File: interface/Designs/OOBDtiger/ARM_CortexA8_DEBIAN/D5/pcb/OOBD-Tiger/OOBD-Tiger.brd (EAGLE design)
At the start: 63.4 x 38.2 mm, 123 parts, among them IC1 ADM3053M, IC2 ADM3053M, IC4 DS3231, U1 SY6280, U10 MP1482DS, U2 SN65HVD230(SO8), U3 SY6280, U6 SN65HVD230(SO8)

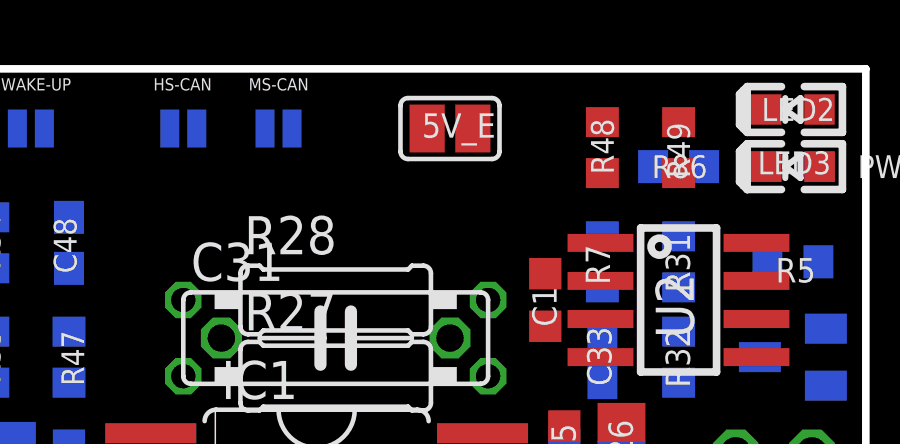
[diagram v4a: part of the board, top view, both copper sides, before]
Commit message: small modifications on schematics/board (signal re-alignment only)
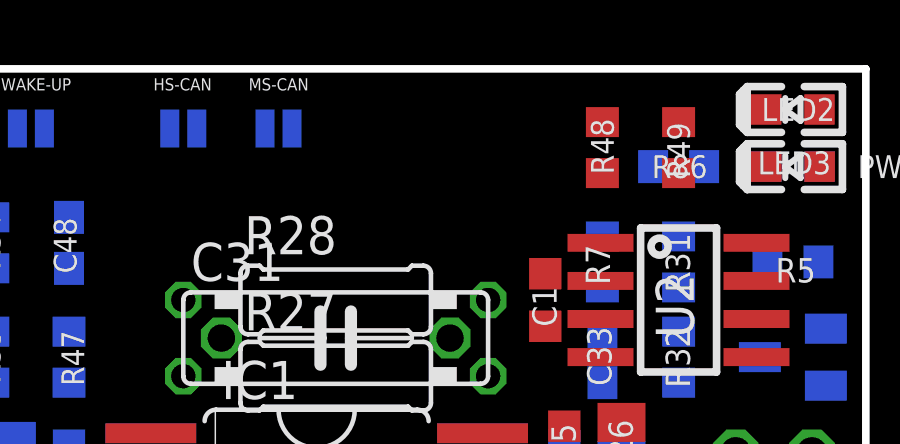
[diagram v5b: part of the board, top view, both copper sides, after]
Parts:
- removed 5V_E: Close, jumper:SJ
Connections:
- net P3_20/LED2 renamed LED2
- removed net N$12: 5V_E.1, C53.1, C54.1, C55.1, C56.1, L11.2, R70.2
- removed net P3_21/LED3: R48.1
- new net LED1: AM3352-SOM-EVB-PLATFORM.4-21, R48.1
- net +5V: now also C53.1, C54.1, C55.1, C56.1, L11.2, R70.2; no longer 5V_E.2
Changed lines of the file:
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@@
 <?xml version="1.0" encoding="utf-8"?>
 <!DOCTYPE eagle SYSTEM "eagle.dtd">
-<eagle version="7.6.0">
+<eagle version="6.4">
 <drawing>
 <settings>
@@
 <layer number="37" name="tTest" color="7" fill="1" visible="no" active="yes"/>
 <layer number="38" name="bTest" color="7" fill="1" visible="no" active="yes"/>
-<layer number="39" name="tKeepout" color="4" fill="11" visible="yes" active="yes"/>
-<layer number="40" name="bKeepout" color="3" fill="11" visible="yes" active="yes"/>
+<layer number="39" name="tKeepout" color="4" fill="11" visible="no" active="yes"/>
+<layer number="40" name="bKeepout" color="3" fill="11" visible="no" active="yes"/>
 <layer number="41" name="tRestrict" color="4" fill="10" visible="no" active="yes"/>
 <layer number="42" name="bRestrict" color="3" fill="10" visible="no" active="yes"/>
@@
 <layer number="46" name="Milling" color="3" fill="1" visible="no" active="yes"/>
 <layer number="47" name="Measures" color="7" fill="1" visible="no" active="yes"/>
-<layer number="48" name="Document" color="5" fill="1" visible="no" active="yes"/>
+<layer number="48" name="Document" color="5" fill="1" visible="yes" active="yes"/>
 <layer number="49" name="Reference" color="7" fill="1" visible="no" active="yes"/>
 <layer number="50" name="dxf" color="7" fill="1" visible="no" active="yes"/>
@@
 <layer number="230" name="230bmp" color="7" fill="1" visible="no" active="yes"/>
 <layer number="231" name="231bmp" color="7" fill="1" visible="no" active="yes"/>
-<layer number="232" name="Eagle3D_PG2" color="7" fill="1" visible="yes" active="yes"/>
-<layer number="233" name="Eagle3D_PG3" color="7" fill="1" visible="yes" active="yes"/>
+<layer number="232" name="Eagle3D_PG2" color="7" fill="1" visible="no" active="yes"/>
+<layer number="233" name="Eagle3D_PG3" color="7" fill="1" visible="no" active="yes"/>
 <layer number="248" name="Housing" color="7" fill="1" visible="no" active="yes"/>
 <layer number="249" name="Edge" color="7" fill="1" visible="no" active="yes"/>
@@
 <wire x1="0" y1="38.184" x2="63.391" y2="38.184" width="0.254" layer="20"/>
 <wire x1="63.391" y1="38.184" x2="63.391" y2="0" width="0.254" layer="20"/>
-<wire x1="55" y1="0" x2="55" y2="45" width="0.254" layer="48" style="shortdash"/>
-<wire x1="0" y1="45" x2="55" y2="45" width="0.254" layer="48" style="shortdash"/>
 <polygon width="0.4064" layer="41">
 <vertex x="41.5925" y="7.62"/>
@@
 <pass name="Default">
 <param name="RoutingGrid" value="50mil"/>
-<param name="AutoGrid" value="1"/>
-<param name="Efforts" value="2"/>
-<param name="TopRouterVariant" value="1"/>
 <param name="tpViaShape" value="round"/>
-<param name="PrefDir.1" value="a"/>
+<param name="PrefDir.1" value="|"/>
 <param name="PrefDir.2" value="0"/>
 <param name="PrefDir.3" value="0"/>
@@
 <param name="PrefDir.14" value="0"/>
 <param name="PrefDir.15" value="0"/>
-<param name="PrefDir.16" value="a"/>
+<param name="PrefDir.16" value="-"/>
 <param name="cfVia" value="8"/>
 <param name="cfNonPref" value="5"/>
@@
 <attribute name="NAME" x="28.956" y="18.669" size="0.762" layer="25" font="vector" ratio="11"/>
 <attribute name="VALUE" x="28.448" y="18.923" size="0.4064" layer="27" ratio="20"/>
-</element>
-<element name="5V_E" library="jumper" package="SJ" value="Close" x="49.53" y="36.195" smashed="yes" rot="R180">
-<attribute name="NAME" x="51.054" y="36.703" size="0.8128" layer="25" font="vector" ratio="11" rot="R180"/>
-<attribute name="VALUE" x="50.5269" y="36.703" size="0.4064" layer="27" rot="R180"/>
-<attribute name="VALUE" x="50.419" y="36.068" size="0.4064" layer="27" ratio="20" rot="R180"/>
 </element>
 <element name="C51" library="SparkFun-Capacitors" package="PANASONIC_D" value="470uF/25V/LOWESR/105C" x="11.43" y="19.05" smashed="yes" rot="R270">
@@
 <contactref element="C6" pad="1"/>
 <contactref element="U1" pad="5"/>
-<contactref element="5V_E" pad="2"/>
 <contactref element="R86" pad="1"/>
 <contactref element="AM3352-SOM-EVB-PLATFORM" pad="3-1"/>
@@
 <contactref element="IC2" pad="6"/>
 <contactref element="OOBDPICAN" pad="1"/>
-<wire x1="48.768" y1="36.195" x2="58" y2="34.925" width="0" layer="19" extent="1-16"/>
-<wire x1="39.5558" y1="20.955" x2="48.768" y2="36.195" width="0" layer="19" extent="1-16"/>
+<contactref element="L11" pad="2"/>
+<contactref element="C53" pad="1"/>
+<contactref element="R70" pad="2"/>
+<contactref element="C54" pad="1"/>
+<contactref element="C55" pad="1"/>
+<contactref element="C56" pad="1"/>
+<wire x1="39.5558" y1="20.955" x2="58" y2="34.925" width="0" layer="19" extent="16-16"/>
 <wire x1="39.5558" y1="19.685" x2="39.5558" y2="20.955" width="0" layer="19" extent="1-16"/>
 <wire x1="36.83" y1="20.56" x2="39.5558" y2="20.955" width="0" layer="19" extent="16-16"/>
@@
 <wire x1="34.925" y1="20.685" x2="36.83" y2="20.56" width="0" layer="19" extent="16-16"/>
 <wire x1="34.925" y1="19.955" x2="34.925" y2="20.685" width="0" layer="19" extent="1-16"/>
-<wire x1="28.095" y1="14.195" x2="34.925" y2="19.955" width="0" layer="19" extent="1-16"/>
+<wire x1="30.695" y1="19.05" x2="34.925" y2="19.955" width="0" layer="19" extent="1-1"/>
+<wire x1="27.52" y1="19.05" x2="30.695" y2="19.05" width="0" layer="19" extent="1-1"/>
+<wire x1="24.345" y1="19.05" x2="27.52" y2="19.05" width="0" layer="19" extent="1-1"/>
+<wire x1="21.17" y1="19.05" x2="24.345" y2="19.05" width="0" layer="19" extent="1-1"/>
+<wire x1="21.17" y1="21.59" x2="21.17" y2="19.05" width="0" layer="19" extent="1-1"/>
+<wire x1="28.095" y1="14.195" x2="27.52" y2="19.05" width="0" layer="19" extent="1-16"/>
+<wire x1="23.57" y1="13.335" x2="28.095" y2="14.195" width="0" layer="19" extent="1-16"/>
 <wire x1="27.94" y1="6.477" x2="28.095" y2="14.195" width="0" layer="19" extent="1-16"/>
 <wire x1="30.48" y1="1.905" x2="27.94" y2="6.477" width="0" layer="19" extent="1-1"/>
-<wire x1="12.7301" y1="25.085" x2="28.095" y2="14.195" width="0" layer="19" extent="16-16"/>
+<wire x1="12.7301" y1="25.085" x2="21.17" y2="21.59" width="0" layer="19" extent="1-16"/>
 <wire x1="9.285" y1="33.655" x2="12.7301" y2="25.085" width="0" layer="19" extent="16-16"/>
 <wire x1="5.0499" y1="35.245" x2="9.285" y2="33.655" width="0" layer="19" extent="1-16"/>
@@
 <wire x1="11.43" y1="2.413" x2="14.315" y2="13.485" width="0" layer="19" extent="1-16"/>
 </signal>
-<signal name="P3_21/LED3">
-<contactref element="R48" pad="1"/>
-</signal>
-<signal name="P3_20/LED2">
+<signal name="LED2">
 <contactref element="R49" pad="1"/>
 <contactref element="AM3352-SOM-EVB-PLATFORM" pad="4-23"/>
@@
 <contactref element="PWR_LED" pad="A"/>
 <wire x1="56.3" y1="34.925" x2="60.071" y2="34.925" width="0" layer="19" extent="16-16"/>
-</signal>
-<signal name="N$12" class="1">
-<contactref element="L11" pad="2"/>
-<contactref element="C53" pad="1"/>
-<contactref element="R70" pad="2"/>
-<contactref element="C54" pad="1"/>
-<contactref element="5V_E" pad="1"/>
-<contactref element="C55" pad="1"/>
-<contactref element="C56" pad="1"/>
-<wire x1="30.695" y1="19.05" x2="50.292" y2="36.195" width="0" layer="19" extent="1-1"/>
-<wire x1="27.52" y1="19.05" x2="30.695" y2="19.05" width="0" layer="19" extent="1-1"/>
-<wire x1="24.345" y1="19.05" x2="27.52" y2="19.05" width="0" layer="19" extent="1-1"/>
-<wire x1="21.17" y1="19.05" x2="24.345" y2="19.05" width="0" layer="19" extent="1-1"/>
-<wire x1="21.17" y1="21.59" x2="21.17" y2="19.05" width="0" layer="19" extent="1-1"/>
-<wire x1="23.57" y1="13.335" x2="24.345" y2="19.05" width="0" layer="19" extent="1-1"/>
 </signal>
 <signal name="N$5">
@@
 <wire x1="57.15" y1="10.58" x2="44.265" y2="36.195" width="0" layer="19" extent="16-16"/>
 </signal>
+<signal name="LED1">
+<contactref element="AM3352-SOM-EVB-PLATFORM" pad="4-21"/>
+<contactref element="R48" pad="1"/>
+<wire x1="15.24" y1="6.477" x2="54.61" y2="34.71" width="0" layer="19" extent="1-1"/>
+</signal>
 </signals>
-<errors>
-</errors>
 </board>
 </drawing>

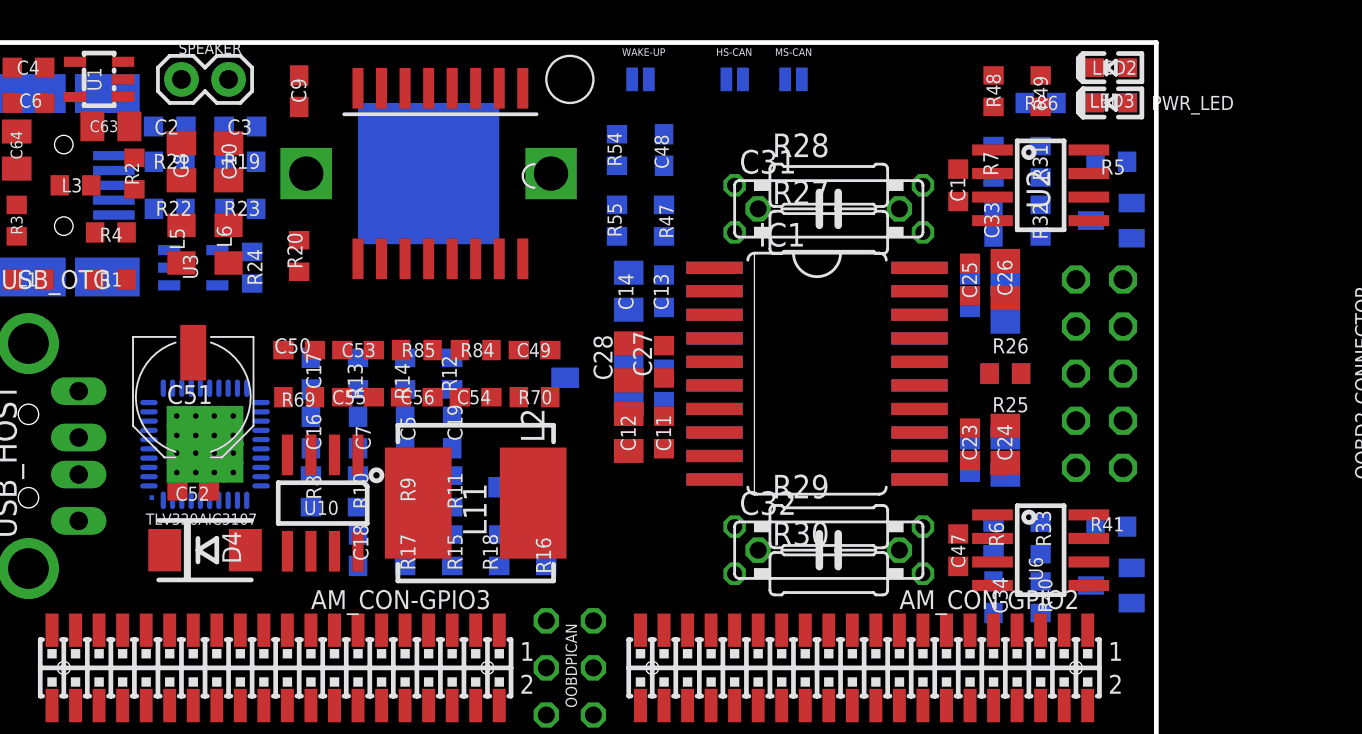
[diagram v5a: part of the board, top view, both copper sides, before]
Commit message: CAN-Transceiver SN65HVD230 shift to left from adm3053
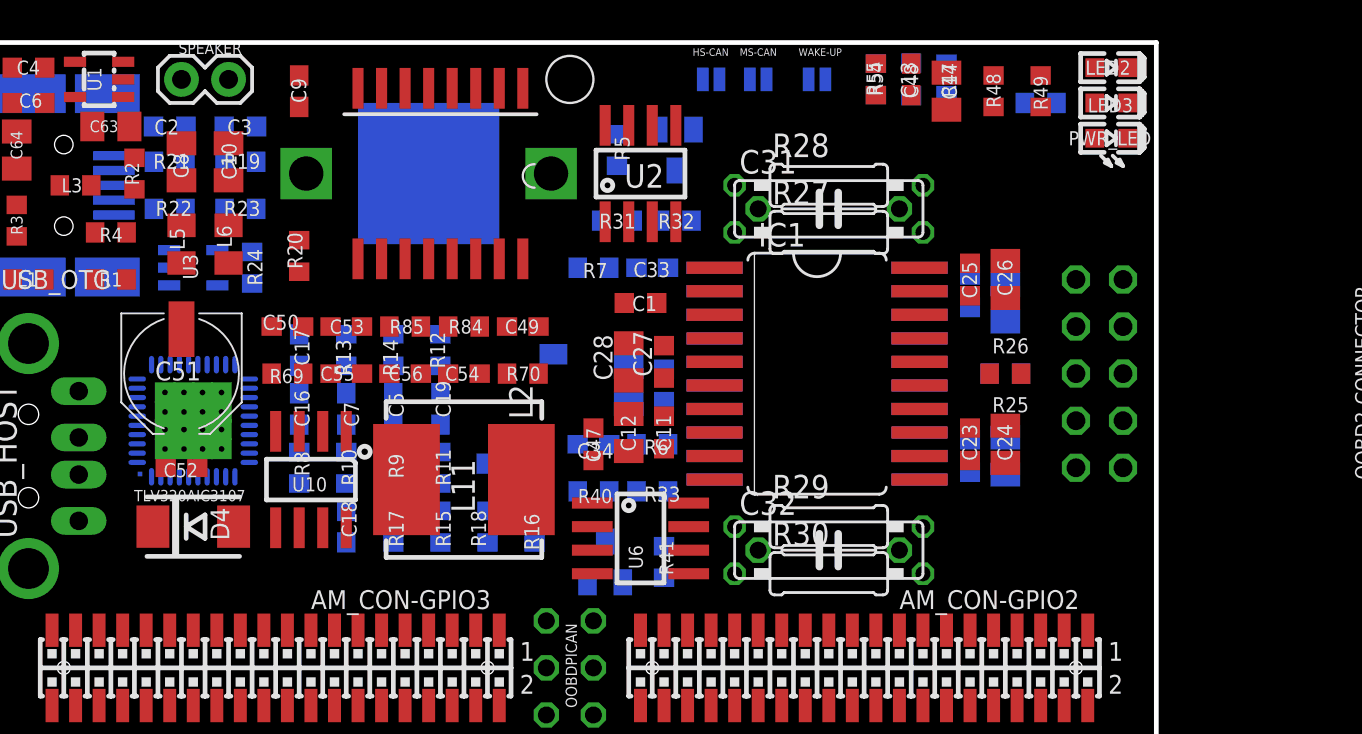
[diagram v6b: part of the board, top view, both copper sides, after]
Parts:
- moved D1 27.3 mm to (33.7, 10.2), turned to 0 degrees
- moved R5 26.7 mm to (34.3, 32.4), turned to 270 degrees
- moved R40 24.8 mm to (33.0, 14.0), turned to 0 degrees
- moved R41 24.2 mm to (36.8, 10.2), turned to 270 degrees
- moved D2 23.8 mm to (37.5, 32.4), turned to 180 degrees
- moved C34 23.1 mm to (33.0, 16.5), turned to 180 degrees
- moved R31 23.1 mm to (34.3, 28.6), turned to 180 degrees
- moved R7 22.3 mm to (33.0, 26.0), turned to 0 degrees
- moved U2 21.6 mm to (35.6, 31.1), turned to 0 degrees
- moved U6 21.6 mm to (35.6, 11.4)
- moved R33 21.1 mm to (36.2, 14.0), turned to 0 degrees
- moved C47 20.5 mm to (33.0, 16.5)
- moved C14 20.3 mm to (52.1, 35.6), flipped to the top
- moved R32 19.7 mm to (37.5, 28.6), turned to 180 degrees
- moved R6 19.1 mm to (36.2, 16.5), turned to 0 degrees
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
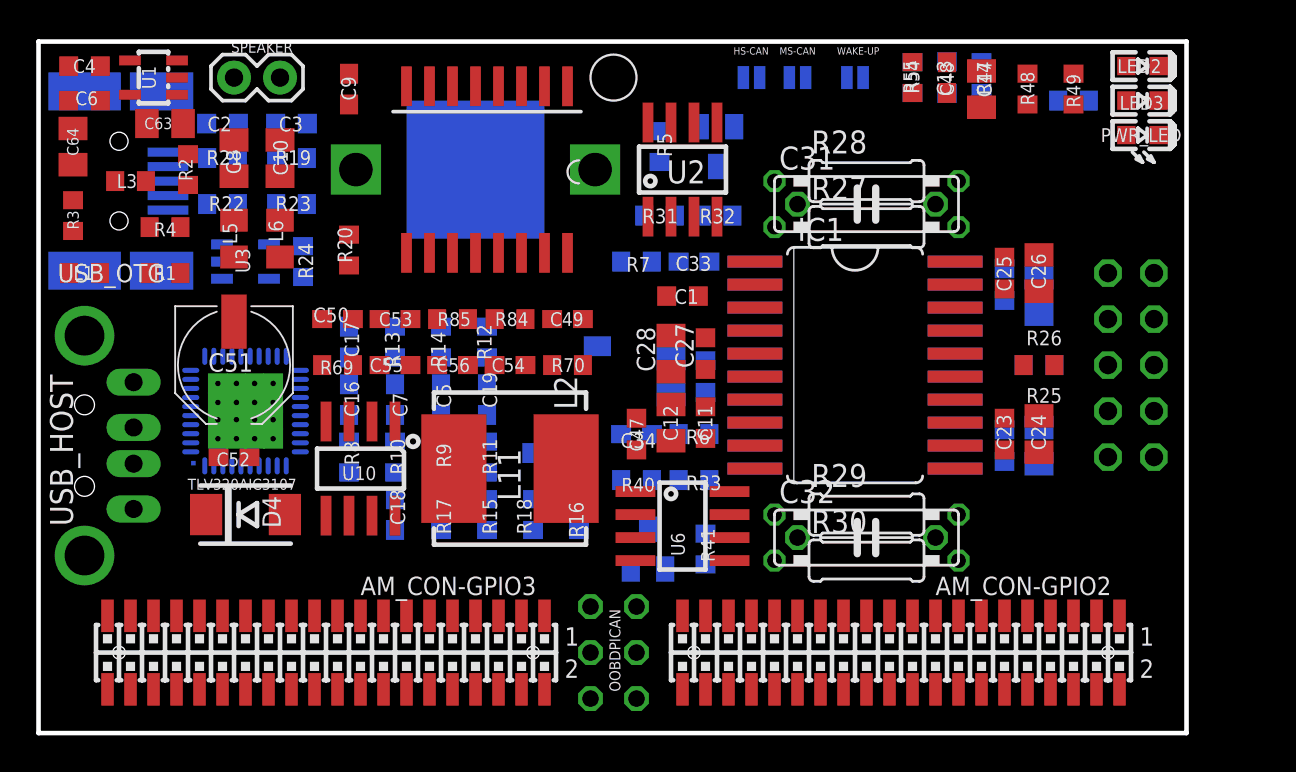
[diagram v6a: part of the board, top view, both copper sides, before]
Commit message: kleinerer Korrekturen
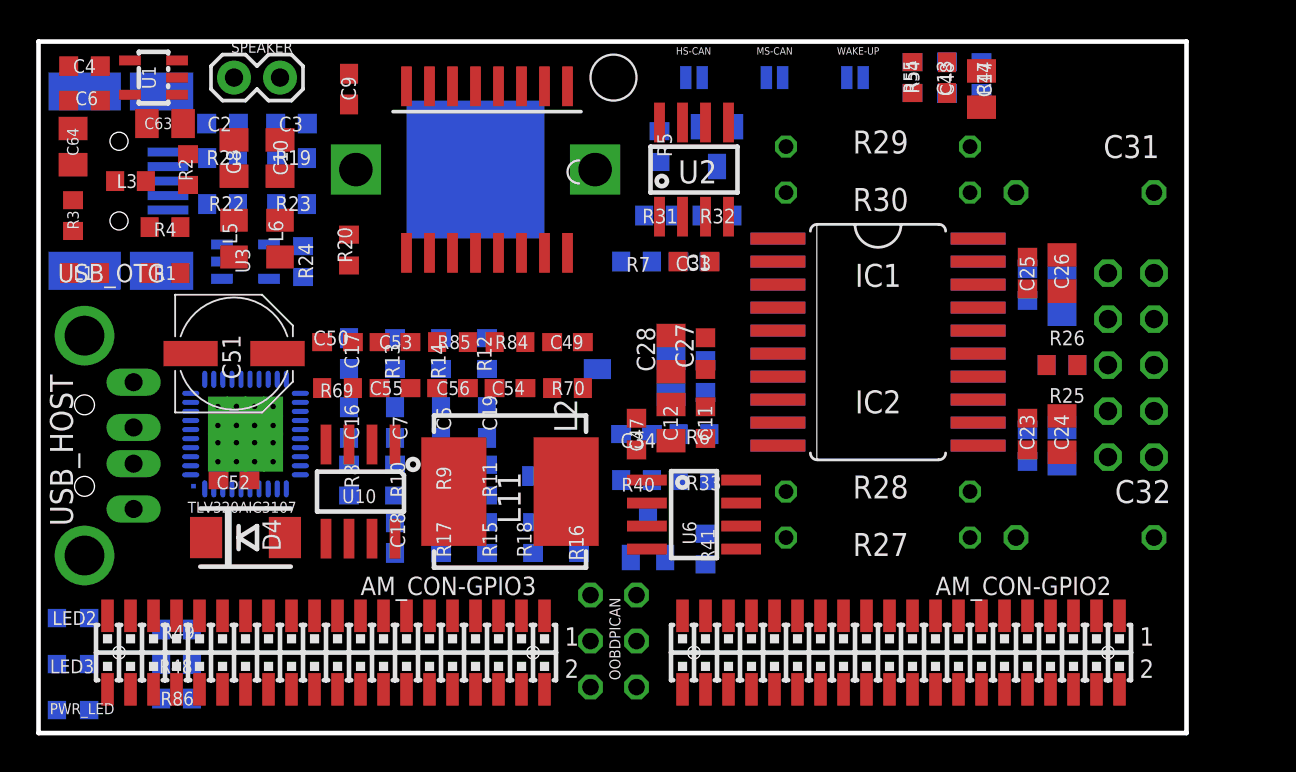
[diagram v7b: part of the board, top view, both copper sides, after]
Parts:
- moved PWR_LED 67.0 mm to (1.91, 1.27), flipped to the bottom
- moved LED3 66.8 mm to (1.91, 3.81), flipped to the bottom
- moved LED2 66.5 mm to (1.91, 6.35), flipped to the bottom
- moved R86 59.5 mm to (7.62, 1.91)
- moved R49 57.8 mm to (7.62, 5.71), flipped to the bottom, turned to 0 degrees
- moved R48 56.7 mm to (7.62, 3.81), flipped to the bottom, turned to 0 degrees
- moved R29 20.3 mm to (46.4, 32.4), flipped to the bottom
- moved R30 20.3 mm to (46.4, 29.8), flipped to the bottom
- moved R27 17.2 mm to (46.4, 10.8), flipped to the bottom
- moved R28 17.2 mm to (46.4, 13.3), flipped to the bottom
- moved C31 12.1 mm to (57.8, 29.8), flipped to the bottom
- moved C32 12.1 mm to (57.8, 10.8), flipped to the bottom
- moved HS-CAN 3.17 mm to (36.2, 36.2)
- moved C1 2.01 mm to (36.2, 26.0)
- moved IC1 1.80 mm to (46.4, 21.6)
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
